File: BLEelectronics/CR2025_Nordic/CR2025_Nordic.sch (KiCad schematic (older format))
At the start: 24 parts, among them Q1 Si2307CDS, U1 LP5907MFX-3.3, U2 BAT-HLD-001, U3 LTC4412xS6, U4 LTC4054LES5-4.2#TRPBF, U5 MX25R6435FM2IL0

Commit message: Update paths for schematic libraries so that they are relative to the project and not computer/deployment dependent.
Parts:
- A1: symbol MCU_Module:Nordic_nRF52840_breakout -> CR2025_Nordic-rescue:Nordic_nRF52840_breakout-MCU_Module
- U3: symbol Power_Management:LTC4412xS6 -> CR2025_Nordic-rescue:LTC4412xS6-Power_Management
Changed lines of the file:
@@
 $EndComp
 $Comp
-L Power_Management:LTC4412xS6 U3
+L CR2025_Nordic-rescue:LTC4412xS6-Power_Management U3
 U 1 1 5E9DE63A
 P 2400 5550
@@
 $EndComp
 $Comp
-L MCU_Module:Nordic_nRF52840_breakout A1
+L CR2025_Nordic-rescue:Nordic_nRF52840_breakout-MCU_Module A1
 U 1 1 5EA6E901
 P 5900 1950

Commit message: Completed Nordic Dongle adaptor. DRC clean. Ready for review
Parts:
- removed U5: MX25R6435FM2IL0, Package_SO:TSSOP-8_4.4x3mm_P0.65mm, symbol Memory_Flash:AT25SF081-XMHD-X
- added H1: MountingHole, MountingHole:MountingHole_2.2mm_M2_Pad, symbol Mechanical:MountingHole
- added IC2: PCF8523T, Package_SO:SOIC-8_3.9x4.9mm_P1.27mm, symbol Timer_RTC:PCF8523T
- added IC3: MX25R6435FM2IL0, 0my_footprints:MX25R6435FM2IL0, symbol mx25R6435FM2IL:MX25R6435FM2IL0
- added JP1, JP2: Jumper_2_Open, Jumper:SolderJumper-2_P1.3mm_Open_RoundedPad1.0x1.5mm, symbol Jumper:Jumper_2_Open
- added R8, R9: 4.7K, Resistor_SMD:R_0603_1608Metric_Pad1.05x0.95mm_HandSolder, symbol Device:R
- IC1: renamed from U3; symbol CR2025_Nordic-rescue:LTC4412xS6-Power_Management -> ltc4412xs6:LTC4412xS6
- J1: renamed from A1; footprint Module:Adafruit_HUZZAH_ESP8266_breakout -> 0my_footprints:Nordic_nRF52840_FeatherHeader; symbol CR2025_Nordic-rescue:Nordic_nRF52840_breakout-MCU_Module -> nordic_nrf52840_breakout:Nordic_nRF52840_breakout; DPN (none) -> 1490-1073-ND; LCSCPN (none) -> -; MFR (none) -> Nordic Semiconductor ASA; MPN (none) -> NRF52840-DONGLE; SIM (none) -> -; SPN (none) -> -; SPR (none) -> -
- R4: DPN - -> RC0201FR-071K69L; MFR - -> Yageo; MPN - -> RC0201FR-07560KL
- R6: DPN - -> YAG2487CT-ND; MFR - -> Yageo; MPN - -> RC0201FR-071K69L
- U1: DPN (none) -> 296-38557-1-ND; LCSCPN (none) -> -; MFR (none) -> Texas Instruments; MPN (none) -> LP5907MFX-3.3; SIM (none) -> -; SPN (none) -> C143028; SPR (none) -> LCSC
- renumbered U4 to IC4
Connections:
- net labels added: CS, RESET, SCL, SCLK, SDA, SI, SO, WP
- wire segments 49 -> 58
- no-connect marks 22 -> 14
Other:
- note added: "Confirm no connect\noscillator IO"
- note added: "Confirm no pull-up/down\nresistors for SPI protocol"
- note added: "Do we need a \nSchottky Diode \nhere?"
- note added: "GPIO not marked for any other function or low frequency include P0.13,15,17,20,22, 24"
- note added: "MOSFET is top risk component. \nNo single MOSFET in datasheet."
- note added: "P1.13 is a low frequency GPIO (<10kHz)"
- note added: "Real time clock module with i2c interface"
- note added: "SPI interface flash memory with SPI"
- note added: "TVS diode \nfor ESD\nprotection"
- note added: "TVS diode for ESD"
- note removed: "SPI interface flash memory PLACE HOLDER"
- moved on the sheet: C4, C5, D3, U1

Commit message: Updated schematic: jumper bypass MOSFET, clock out to header, WP moved to fast IO, fixed library refs, ass spare MOSFET from LTC4412 datasheet.
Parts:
- added D4: D_Schottky, Diode_SMD:D_SOD-123F, symbol Device:D_Schottky
- added J4: Conn_01x01_Female, Connector_PinHeader_2.54mm:PinHeader_1x01_P2.54mm_Vertical, symbol Connector:Conn_01x01_Female
- added JP3, JP4: Jumper_2_Open, Jumper:SolderJumper-2_P1.3mm_Open_RoundedPad1.0x1.5mm, symbol Jumper:Jumper_2_Open
- added Q2: Si7463DP, Package_SO:PowerPAK_SO-8_Single, symbol Si7463DP:Si7463DP
- IC1: symbol ltc4412xs6:LTC4412xS6 -> CR2025_Nordic-rescue:LTC4412xS6-ltc4412xs6
- IC3: symbol mx25R6435FM2IL:MX25R6435FM2IL0 -> CR2025_Nordic-rescue:MX25R6435FM2IL0-mx25R6435FM2IL
- J1: symbol nordic_nrf52840_breakout:Nordic_nRF52840_breakout -> CR2025_Nordic-rescue:Nordic_nRF52840_breakout-nordic_nrf52840_breakout
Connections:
- wire segments 58 -> 70
- no-connect marks 14 -> 13
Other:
- note added: "Added a Schottkey Diode"
- note added: "GPIO not marked for any other function or low frequency include P0.13, 15, 17, 20, 22, 24, P1.00"
- note added: "P1.15 is a low frequency GPIO (<10kHz)"
- note removed: "Do we need a \nSchottky Diode \nhere?"
- note removed: "GPIO not marked for any other function or low frequency include P0.13,15,17,20,22, 24"
- note removed: "MOSFET is top risk component. \nNo single MOSFET in datasheet."
- note removed: "P1.13 is a low frequency GPIO (<10kHz)"
- moved on the sheet: C1, C2, C3, C4, C5, D1, D3, IC4, Q1, R1, R2, R3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

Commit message: tweaks to nordic dongle adaptor.
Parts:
- removed D1, D2: TPD1E10B06DPYR, DIODFN100X60X45-2N, symbol TPD1E10B06DPYR:TPD1E10B06DPYR
- added U3, U4: ESD401, 0my_footprints:ESD401DPYR, symbol ESD401DPYR:ESD401DPYR
- C3, C4, C5: DPN 587-2786-6-ND -> 1276-1862-1-ND; MPN CL10B105KA8NNNC -> CL10A105KO5LNNC
- H1, J4: DPN (none) -> -; LCSCPN (none) -> -; MFR (none) -> -; MPN (none) -> -; SIM (none) -> -; SPN (none) -> -; SPR (none) -> -
- Q2: DPN (none) -> SI7463DP-T1-GE3; LCSCPN (none) -> -; MFR (none) -> Vishay Siliconix; MPN (none) -> SI7463DP-T1-GE3; SIM (none) -> -; SPN (none) -> -; SPR (none) -> -
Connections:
- wire segments 70 -> 69

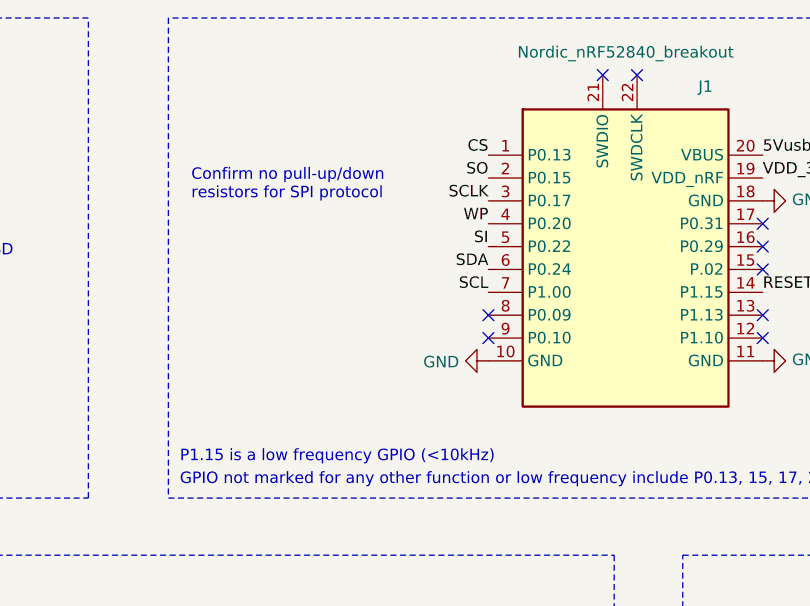
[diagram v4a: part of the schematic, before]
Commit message: updated CR2025_Nordic adaptor BOM.
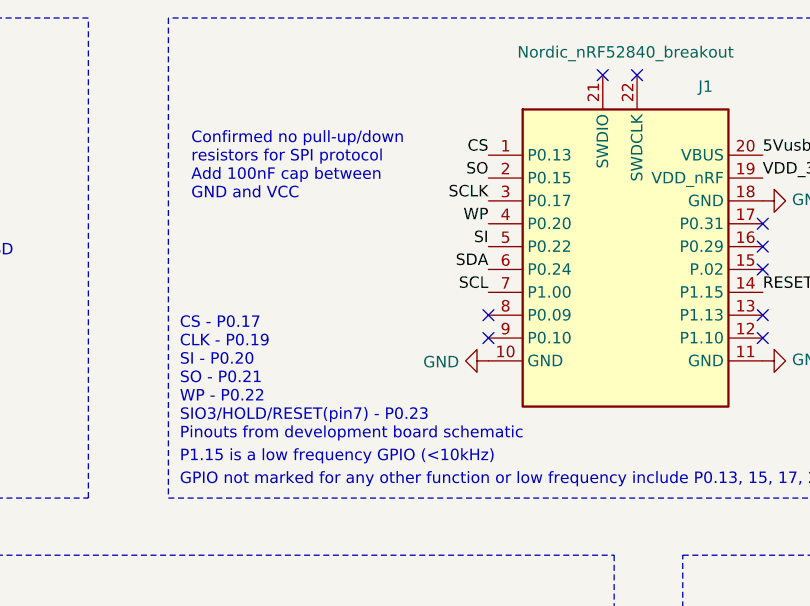
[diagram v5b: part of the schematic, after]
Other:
- note added: "CS - P0.17\nCLK - P0.19\nSI - P0.20\nSO - P0.21\nWP - P0.22\nSIO3/HOLD/RESET(pin7) - P0.23\nPinouts from development board schematic\n"
- note added: "Confirmed no pull-up/down\nresistors for SPI protocol\nAdd 100nF cap between \nGND and VCC"
- note removed: "Confirm no pull-up/down\nresistors for SPI protocol"
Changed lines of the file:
@@
 WP
 Text Notes 4000 1700 0    50   ~ 0
-Confirm no pull-up/down\nresistors for SPI protocol
+Confirmed no pull-up/down\nresistors for SPI protocol\nAdd 100nF cap between \nGND and VCC
 Text Label 6650 3550 0    50   ~ 0
 VDD_3V
@@
 Wire Wire Line
 	2200 1700 2850 1700
+Text Notes 3950 2750 0    50   ~ 0
+CS - P0.17\nCLK - P0.19\nSI - P0.20\nSO - P0.21\nWP - P0.22\nSIO3/HOLD/RESET(pin7) - P0.23\nPinouts from development board schematic\n
 $EndSCHEMATC

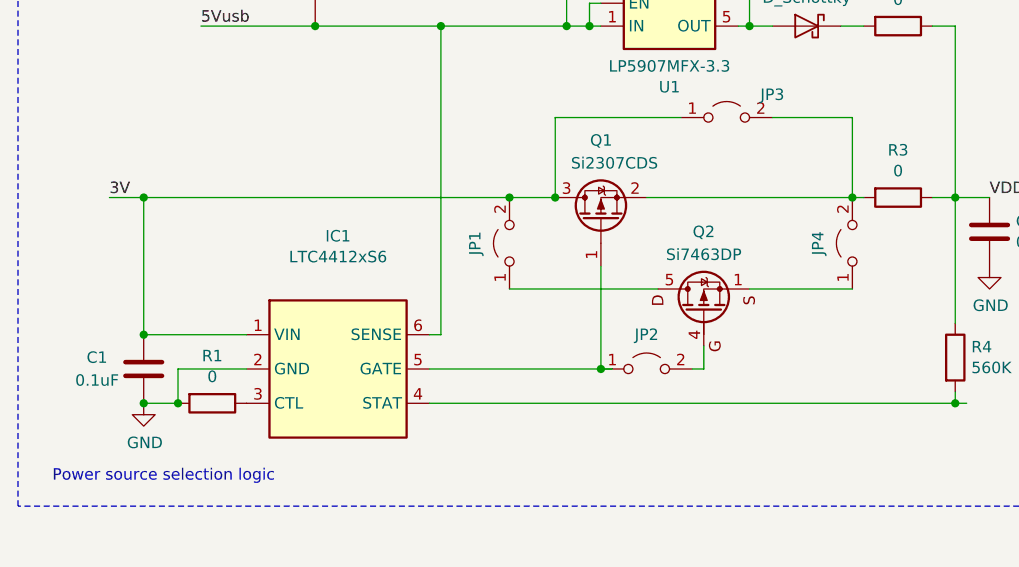
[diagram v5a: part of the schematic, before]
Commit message: Expensive samsung capacitor removed
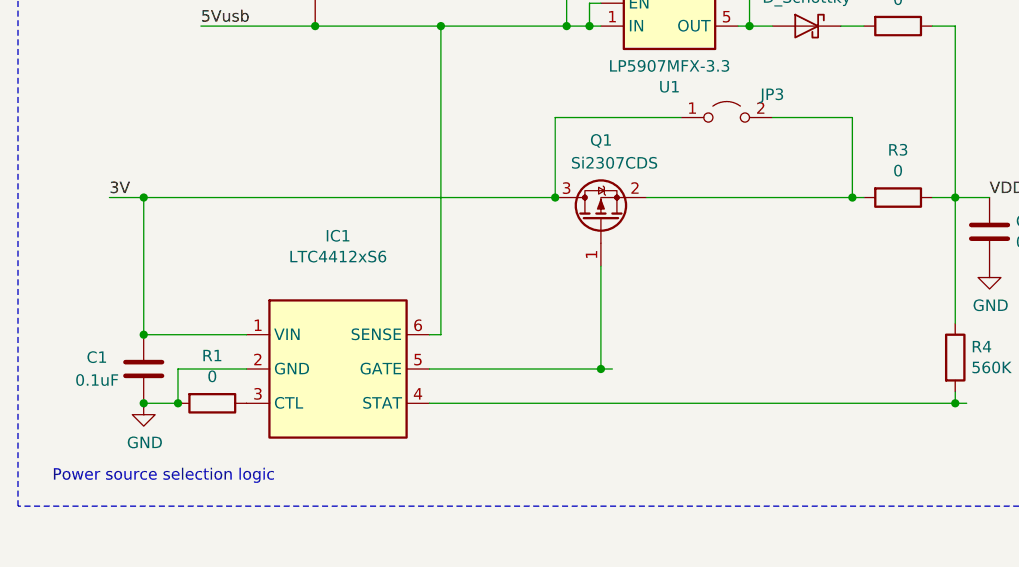
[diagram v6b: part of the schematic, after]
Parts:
- removed JP1, JP2, JP4: Jumper_2_Open, Jumper:SolderJumper-2_P1.3mm_Open_RoundedPad1.0x1.5mm, symbol Jumper:Jumper_2_Open
- removed Q2: Si7463DP, Package_SO:PowerPAK_SO-8_Single, symbol Si7463DP:Si7463DP
- C4, C5: DPN 1276-1862-1-ND -> 445-1416-1-ND; MFR Samsung -> TDK Corporation; MPN CL10A105KO5LNNC -> C1608X5R1C105K080AA
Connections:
- wire segments 69 -> 64
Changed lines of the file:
@@
 F 1 "1uF" H 3565 3805 50  0000 L CNN
 F 2 "Capacitor_SMD:C_0603_1608Metric_Pad1.05x0.95mm_HandSolder" H 3488 3700 50  0001 C CNN
-F 3 "http://www.samsungsem.com/kr/support/product-search/mlcc/CL10A105KO5LNNC.jsp" H 3450 3850 50  0001 C CNN
-F 4 "Samsung" H -5300 2200 50  0001 C CNN "MFR"
-F 5 "CL10A105KO5LNNC" H -5300 2200 50  0001 C CNN "MPN"
-F 6 "1276-1862-1-ND" H -5300 2200 50  0001 C CNN "DPN"
+F 3 "https://product.tdk.com/info/en/catalog/datasheets/mlcc_commercial_general_en.pdf?ref_disty=digikey" H 3450 3850 50  0001 C CNN
+F 4 "TDK Corporation" H -5300 2200 50  0001 C CNN "MFR"
+F 5 "C1608X5R1C105K080AA" H -5300 2200 50  0001 C CNN "MPN"
+F 6 "445-1416-1-ND" H -5300 2200 50  0001 C CNN "DPN"
 F 7 "-" H -5300 2200 50  0001 C CNN "LCSCPN"
 F 8 "-" H -5300 2200 50  0001 C CNN "SPR"
@@
 F 1 "1uF" H 4365 3805 50  0000 L CNN
 F 2 "Capacitor_SMD:C_0603_1608Metric_Pad1.05x0.95mm_HandSolder" H 4288 3700 50  0001 C CNN
-F 3 "http://www.samsungsem.com/kr/support/product-search/mlcc/CL10A105KO5LNNC.jsp" H 4250 3850 50  0001 C CNN
-F 4 "Samsung" H -4500 2200 50  0001 C CNN "MFR"
-F 5 "CL10A105KO5LNNC" H -4500 2200 50  0001 C CNN "MPN"
-F 6 "1276-1862-1-ND" H -4500 2200 50  0001 C CNN "DPN"
+F 3 "https://product.tdk.com/info/en/catalog/datasheets/mlcc_commercial_general_en.pdf?ref_disty=digikey" H 4250 3850 50  0001 C CNN
+F 4 "TDK Corporation" H -4500 2200 50  0001 C CNN "MFR"
+F 5 "C1608X5R1C105K080AA" H -4500 2200 50  0001 C CNN "MPN"
+F 6 "445-1416-1-ND" H -4500 2200 50  0001 C CNN "DPN"
 F 7 "-" H -4500 2200 50  0001 C CNN "LCSCPN"
 F 8 "-" H -4500 2200 50  0001 C CNN "SPR"
@@
 	1    7950 4350
 	0    1    1    0
-$EndComp
-$Comp
-L Si7463DP:Si7463DP Q2
-U 1 1 5EAE0222
-P 4050 5650
-F 0 "Q2" V 4450 5650 50  0000 C CNN
-F 1 "Si7463DP" V 4350 5650 50  0000 C CNN
-F 2 "Package_SO:PowerPAK_SO-8_Single" H 4300 5575 50  0001 L CIN
-F 3 "http://www.vishay.com/docs/72440/si7463dp.pdf" H 4050 5650 50  0001 L CNN
-F 4 "Vishay Siliconix" H 0   0   50  0001 C CNN "MFR"
-F 5 "SI7463DP-T1-GE3" H 0   0   50  0001 C CNN "MPN"
-F 6 "SI7463DP-T1-GE3" H 0   0   50  0001 C CNN "DPN"
-F 7 "-" H 0   0   50  0001 C CNN "LCSCPN"
-F 8 "-" H 0   0   50  0001 C CNN "SPR"
-F 9 "-" H 0   0   50  0001 C CNN "SPN"
-F 10 "-" H 0   0   50  0001 C CNN "SIM"
-	1    4050 5650
-	0    1    -1   0
-$EndComp
-$Comp
-L si2307cds:Si2307CDS Q1
-U 1 1 5E9CEE32
-P 3600 5200
-F 0 "Q1" V 3950 5150 50  0000 L CNN
-F 1 "Si2307CDS" V 3850 4950 50  0000 L CNN
-F 2 "Package_TO_SOT_SMD:SOT-23" H 3800 5125 50  0001 L CIN
-F 3 "http://www.vishay.com/docs/68768/si2307cds.pdf" H 3600 5200 50  0001 L CNN
-F 4 "Vishay Siliconix" H -2550 3350 50  0001 C CNN "MFR"
-F 5 "SI2307CDS-T1-GE3" H -2550 3350 50  0001 C CNN "MPN"
-F 6 "SI2307CDS-T1-GE3CT-ND" H -2550 3350 50  0001 C CNN "DPN"
-F 7 "-" H -2550 3350 50  0001 C CNN "LCSCPN"
-F 8 "-" H -2550 3350 50  0001 C CNN "SPR"
-F 9 "-" H -2550 3350 50  0001 C CNN "SPN"
-F 10 "-" H -2550 3350 50  0001 C CNN "SIM"
-	1    3600 5200
-	0    -1   -1   0
-$EndComp
-$Comp
-L Jumper:Jumper_2_Open JP2
-U 1 1 5EA1D258
-P 3800 5850
-F 0 "JP2" H 3800 6000 50  0000 C CNN
-F 1 "Jumper_2_Open" H 3800 5994 50  0001 C CNN
-F 2 "Jumper:SolderJumper-2_P1.3mm_Open_RoundedPad1.0x1.5mm" H 3800 5850 50  0001 C CNN
-F 3 "~" H 3800 5850 50  0001 C CNN
-F 4 "-" H -2900 3750 50  0001 C CNN "MFR"
-F 5 "-" H -2900 3750 50  0001 C CNN "MPN"
-F 6 "-" H -2900 3750 50  0001 C CNN "DPN"
-F 7 "-" H -2900 3750 50  0001 C CNN "LCSCPN"
-F 8 "-" H -2900 3750 50  0001 C CNN "SPR"
-F 9 "-" H -2900 3750 50  0001 C CNN "SPN"
-F 10 "-" H -2900 3750 50  0001 C CNN "SIM"
-	1    3800 5850
-	1    0    0    -1
-$EndComp
-$Comp
-L Jumper:Jumper_2_Open JP1
-U 1 1 5EA32B98
-P 3200 5300
-F 0 "JP1" H 3200 5450 50  0000 C CNN
-F 1 "Jumper_2_Open" H 3200 5444 50  0001 C CNN
-F 2 "Jumper:SolderJumper-2_P1.3mm_Open_RoundedPad1.0x1.5mm" H 3200 5300 50  0001 C CNN
-F 3 "~" H 3200 5300 50  0001 C CNN
-F 4 "-" H -3500 3200 50  0001 C CNN "MFR"
-F 5 "-" H -3500 3200 50  0001 C CNN "MPN"
-F 6 "-" H -3500 3200 50  0001 C CNN "DPN"
-F 7 "-" H -3500 3200 50  0001 C CNN "LCSCPN"
-F 8 "-" H -3500 3200 50  0001 C CNN "SPR"
-F 9 "-" H -3500 3200 50  0001 C CNN "SPN"
-F 10 "-" H -3500 3200 50  0001 C CNN "SIM"
-	1    3200 5300
-	0    -1   -1   0
-$EndComp
-$Comp
-L Jumper:Jumper_2_Open JP4
-U 1 1 5EA4C3C0
-P 4700 5300
-F 0 "JP4" H 4700 5450 50  0000 C CNN
-F 1 "Jumper_2_Open" H 4700 5444 50  0001 C CNN
-F 2 "Jumper:SolderJumper-2_P1.3mm_Open_RoundedPad1.0x1.5mm" H 4700 5300 50  0001 C CNN
-F 3 "~" H 4700 5300 50  0001 C CNN
-F 4 "-" H -2000 3200 50  0001 C CNN "MFR"
-F 5 "-" H -2000 3200 50  0001 C CNN "MPN"
-F 6 "-" H -2000 3200 50  0001 C CNN "DPN"
-F 7 "-" H -2000 3200 50  0001 C CNN "LCSCPN"
-F 8 "-" H -2000 3200 50  0001 C CNN "SPR"
-F 9 "-" H -2000 3200 50  0001 C CNN "SPN"
-F 10 "-" H -2000 3200 50  0001 C CNN "SIM"
-	1    4700 5300
-	0    -1   -1   0
 $EndComp
 $Comp
@@
 	2850 5850 3600 5850
 Wire Wire Line
-	3200 5100 3400 5100
-Wire Wire Line
-	1600 5100 3200 5100
-Wire Wire Line
 	3800 5100 4700 5100
-Wire Wire Line
-	3600 5400 3600 5850
-Wire Wire Line
-	3200 5500 3850 5500
-Wire Wire Line
-	4250 5500 4700 5500
-Wire Wire Line
-	4050 5750 4050 5850
-Wire Wire Line
-	4050 5850 4000 5850
 Wire Wire Line
 	2900 4350 3450 4350
@@
 Connection ~ 1600 5100
 Connection ~ 3600 5850
-Connection ~ 3200 5100
 Connection ~ 4700 5100
-Connection ~ 3400 5100
 Connection ~ 2900 4350
 Connection ~ 5150 6000
@@
 Text Notes 3950 2750 0    50   ~ 0
 CS - P0.17\nCLK - P0.19\nSI - P0.20\nSO - P0.21\nWP - P0.22\nSIO3/HOLD/RESET(pin7) - P0.23\nPinouts from development board schematic\n
+Connection ~ 3400 5100
+Wire Wire Line
+	3600 5400 3600 5850
+$Comp
+L si2307cds:Si2307CDS Q1
+U 1 1 5E9CEE32
+P 3600 5200
+F 0 "Q1" V 3950 5150 50  0000 L CNN
+F 1 "Si2307CDS" V 3850 4950 50  0000 L CNN
+F 2 "Package_TO_SOT_SMD:SOT-23" H 3800 5125 50  0001 L CIN
+F 3 "http://www.vishay.com/docs/68768/si2307cds.pdf" H 3600 5200 50  0001 L CNN
+F 4 "Vishay Siliconix" H -2550 3350 50  0001 C CNN "MFR"
+F 5 "SI2307CDS-T1-GE3" H -2550 3350 50  0001 C CNN "MPN"
+F 6 "SI2307CDS-T1-GE3CT-ND" H -2550 3350 50  0001 C CNN "DPN"
+F 7 "-" H -2550 3350 50  0001 C CNN "LCSCPN"
+F 8 "-" H -2550 3350 50  0001 C CNN "SPR"
+F 9 "-" H -2550 3350 50  0001 C CNN "SPN"
+F 10 "-" H -2550 3350 50  0001 C CNN "SIM"
+	1    3600 5200
+	0    -1   -1   0
+$EndComp
+Wire Wire Line
+	1600 5100 3400 5100
 $EndSCHEMATC

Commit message: CR2025_Nordic BOM Clean
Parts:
- C3: DPN 1276-1862-1-ND -> 445-1416-1-ND; MFR Samsung -> TDK Corporation; MPN CL10A105KO5LNNC -> C1608X5R1C105K080AA
- R8, R9: value 4.7K -> 10K; DPN 311-4.70KHRCT-ND -> 311-10KGRCT-ND; MPN RC0603FR-074K7L -> RC0603JR-0710KL
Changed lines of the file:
@@
 F 2 "Capacitor_SMD:C_0603_1608Metric_Pad1.05x0.95mm_HandSolder" H 8588 1400 50  0001 C CNN
 F 3 "http://www.samsungsem.com/kr/support/product-search/mlcc/CL10A105KO5LNNC.jsp" H 8550 1550 50  0001 C CNN
-F 4 "Samsung" H -200 -100 50  0001 C CNN "MFR"
-F 5 "CL10A105KO5LNNC" H -200 -100 50  0001 C CNN "MPN"
-F 6 "1276-1862-1-ND" H -200 -100 50  0001 C CNN "DPN"
+F 4 "TDK Corporation" H -200 -100 50  0001 C CNN "MFR"
+F 5 "C1608X5R1C105K080AA" H -200 -100 50  0001 C CNN "MPN"
+F 6 "445-1416-1-ND" H -200 -100 50  0001 C CNN "DPN"
 F 7 "-" H -200 -100 50  0001 C CNN "LCSCPN"
 F 8 "-" H -200 -100 50  0001 C CNN "SPR"
@@
 P 6800 3800
 F 0 "R9" H 6870 3846 50  0000 L CNN
-F 1 "4.7K" H 6870 3755 50  0000 L CNN
+F 1 "10K" H 6870 3755 50  0000 L CNN
 F 2 "Resistor_SMD:R_0603_1608Metric_Pad1.05x0.95mm_HandSolder" V 6730 3800 50  0001 C CNN
 F 3 "https://www.yageo.com/upload/media/product/productsearch/datasheet/rchip/PYu-RC_Group_51_RoHS_L_10.pdf" H 6800 3800 50  0001 C CNN
 F 4 "Yageo" H 350 50  50  0001 C CNN "MFR"
-F 5 "RC0603FR-074K7L" H 350 50  50  0001 C CNN "MPN"
-F 6 "311-4.70KHRCT-ND" H 350 50  50  0001 C CNN "DPN"
+F 5 "RC0603JR-0710KL" H 350 50  50  0001 C CNN "MPN"
+F 6 "311-10KGRCT-ND" H 350 50  50  0001 C CNN "DPN"
 F 7 "-" H 350 50  50  0001 C CNN "LCSCPN"
 F 8 "-" H 350 50  50  0001 C CNN "SPR"
@@
 P 6500 3900
 F 0 "R8" H 6570 3946 50  0000 L CNN
-F 1 "4.7K" H 6570 3855 50  0000 L CNN
+F 1 "10K" H 6570 3855 50  0000 L CNN
 F 2 "Resistor_SMD:R_0603_1608Metric_Pad1.05x0.95mm_HandSolder" V 6430 3900 50  0001 C CNN
 F 3 "https://www.yageo.com/upload/media/product/productsearch/datasheet/rchip/PYu-RC_Group_51_RoHS_L_10.pdf" H 6500 3900 50  0001 C CNN
 F 4 "Yageo" H 50  150 50  0001 C CNN "MFR"
-F 5 "RC0603FR-074K7L" H 50  150 50  0001 C CNN "MPN"
-F 6 "311-4.70KHRCT-ND" H 50  150 50  0001 C CNN "DPN"
+F 5 "RC0603JR-0710KL" H 50  150 50  0001 C CNN "MPN"
+F 6 "311-10KGRCT-ND" H 50  150 50  0001 C CNN "DPN"
 F 7 "-" H 50  150 50  0001 C CNN "LCSCPN"
 F 8 "-" H 50  150 50  0001 C CNN "SPR"
